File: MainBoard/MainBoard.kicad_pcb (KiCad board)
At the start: 6 copper layers, 45 x 45.6 mm, 93 parts, among them J1 KH-TYPE-C-16P, Q1 PMV19XNEAR, Q2 PMV19XNEAR, Q3 PMV19XNEAR, Q4 PMV19XNEAR, U2 SI3477DV-T1-GE3, U3 STM32L496VGY6PTR, U4 FUSB302BMPX, U5 BNO086, U6 TPS63802DLAR, U7 SI3477DV-T1-GE3, U8 BQ25756ERRVR, U9 TCAN332DCNR, Y1 9HT11-32.768KBZF-T

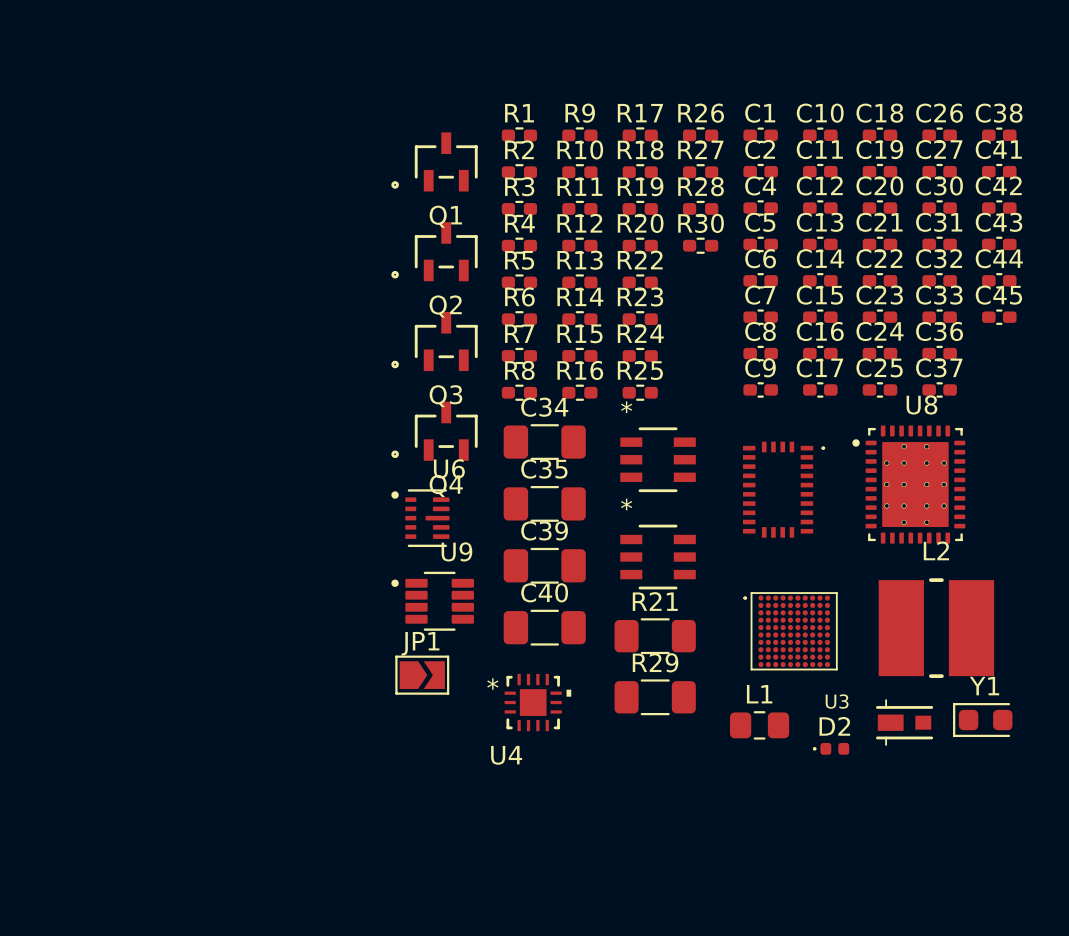
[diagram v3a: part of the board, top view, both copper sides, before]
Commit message: Adding cutoff circuits and others
Added 3.3V and Bat Voltage current sense and cutoff cirucits

Also changed footprints to non-hand solder for 0402

And changed I2C pullups to an array
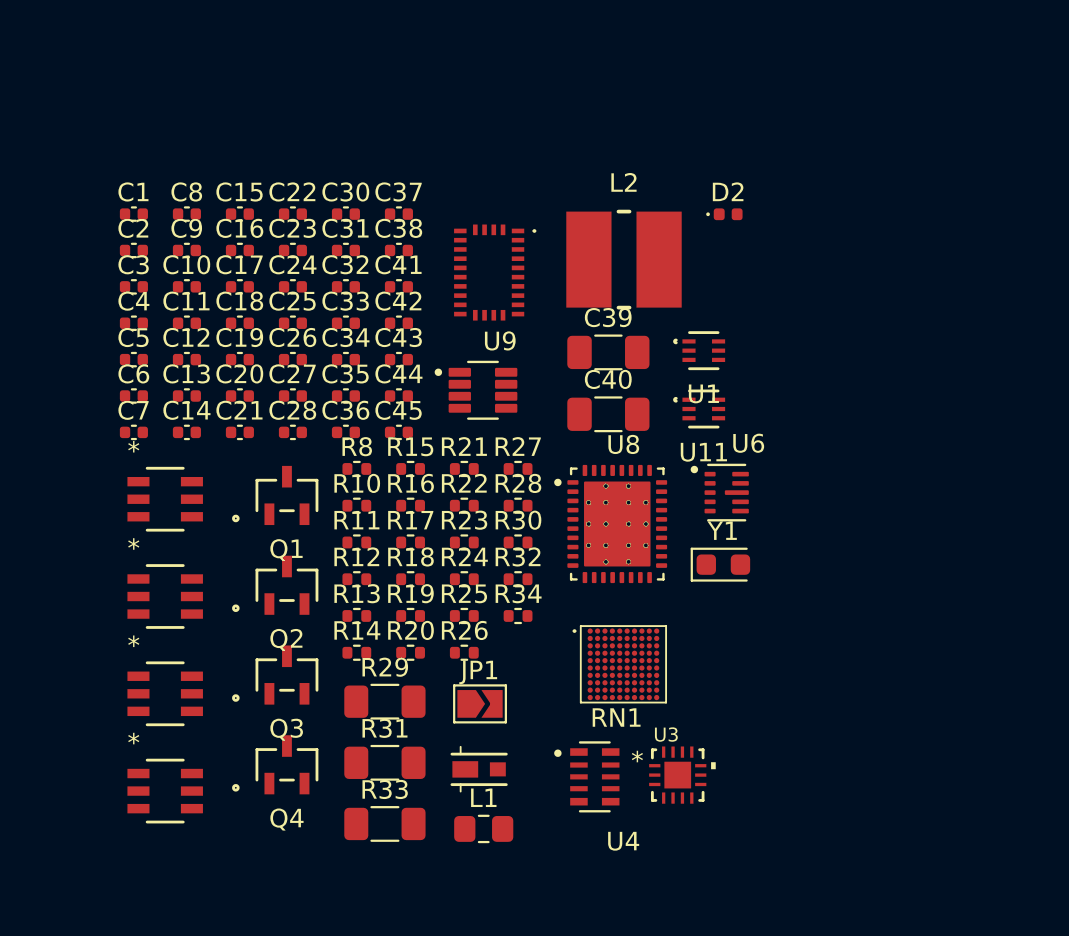
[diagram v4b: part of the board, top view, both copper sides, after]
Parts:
- removed R1, R2, R3, R4, R5, R6, R7, R9: 2.2k, Resistor_SMD:R_0402_1005Metric_Pad0.72x0.64mm_HandSolder
- added C28: 100nF, Capacitor_SMD:C_0402_1005Metric, F.Cu at (131.7, 61.5)
- added C3: 100nF, Capacitor_SMD:C_0402_1005Metric, F.Cu at (123.1, 53.6)
- added R31: 5m, Resistor_SMD:R_1206_3216Metric_Pad1.30x1.75mm_HandSolder, F.Cu at (136.7, 79.4)
- added R32: 100K, Resistor_SMD:R_0402_1005Metric, F.Cu at (143.9, 69.5)
- added R33: 5m, Resistor_SMD:R_1206_3216Metric_Pad1.30x1.75mm_HandSolder, F.Cu at (136.7, 82.7)
- added R34: 100K, Resistor_SMD:R_0402_1005Metric, F.Cu at (143.9, 71.5)
- added RN1: YC158TJR-072K2L, inspirefly:RESCAXE64P320X160X70-10N, F.Cu at (148.0, 80.2)
- added U1: INA185A4IDRLR, inspirefly:SOT_INA185_TEX, F.Cu at (153.9, 57.1)
- added U10: SI3477DV-T1-GE3, inspirefly:SOT_V-T1-GE3_VIS-M, F.Cu at (124.8, 75.7)
- added U11: INA185A4IDRLR, inspirefly:SOT_INA185_TEX, F.Cu at (153.9, 60.3)
- added U12: SI3477DV-T1-GE3, inspirefly:SOT_V-T1-GE3_VIS-M, F.Cu at (124.8, 80.9)
- C1, C10, C11, C12, C13, C14, C15, C16, C17, C18, C19, C2, C20, C21, C22, C23, C24, C25, C26, C27, C30, C31, C32, C33, C36, C37, C38, C4, C41, C42, C43, C44, C45, C5, C6, C7, C8, C9: footprint Capacitor_SMD:C_0402_1005Metric_Pad0.74x0.62mm_HandSolder -> Capacitor_SMD:C_0402_1005Metric
- C34, C35: footprint Capacitor_SMD:C_1206_3216Metric_Pad1.33x1.80mm_HandSolder -> Capacitor_SMD:C_0402_1005Metric
- R10, R11, R12, R13, R14, R15, R16, R17, R18, R19, R20, R22, R23, R24, R25, R26, R27, R28, R30, R8: footprint Resistor_SMD:R_0402_1005Metric_Pad0.72x0.64mm_HandSolder -> Resistor_SMD:R_0402_1005Metric
- R21: footprint Resistor_SMD:R_1206_3216Metric_Pad1.30x1.75mm_HandSolder -> Resistor_SMD:R_0402_1005Metric
- moved C26 37.1 mm to (131.7, 57.6)
- moved C27 37.1 mm to (131.7, 59.6)
- moved C18 36.1 mm to (128.8, 55.6)
- moved C19 36.1 mm to (128.8, 57.6)
- moved C20 36.1 mm to (128.8, 59.6)
- moved C21 36.1 mm to (128.8, 61.5)
- moved C11 35.3 mm to (126.0, 55.6)
- moved C10 35.3 mm to (126.0, 53.6)
- moved C12 35.3 mm to (126.0, 57.6)
- moved C13 35.3 mm to (126.0, 59.6)
- moved C14 35.3 mm to (126.0, 61.5)
- moved C4 34.5 mm to (123.1, 55.6)
- moved C5 34.5 mm to (123.1, 57.6)
- moved C6 34.5 mm to (123.1, 59.6)
- moved C7 34.5 mm to (123.1, 61.5)
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
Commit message: Footprint edits and board setup
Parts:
- removed C24, C25: 22pF, Capacitor_SMD:C_0402_1005Metric
- removed Y1: 9HT11-32.768KBZF-T, Crystal:Crystal_SMD_2012-2Pin_2.0x1.2mm_HandSoldering
- added TP1: BatBeforeCutoff, TestPoint:TestPoint_Pad_D1.0mm, F.Cu at (155.0, 71.9)
- added TP2: Bat+, TestPoint:TestPoint_Pad_D1.0mm, F.Cu at (155.0, 74.9)
- added TP3: 3.3V, TestPoint:TestPoint_Pad_D1.0mm, F.Cu at (158.1, 71.9)
- added TP4: GND, TestPoint:TestPoint_Pad_D1.0mm, F.Cu at (158.1, 74.9)
- added TP5: GND, TestPoint:TestPoint_Pad_D1.0mm, F.Cu at (161.1, 71.9)
- added TP6: GND, TestPoint:TestPoint_Pad_D1.0mm, F.Cu at (161.1, 74.9)
- JP1: footprint Jumper:SolderJumper-2_P1.3mm_Open_TrianglePad1.0x1.5mm -> inspirefly:SmallJumper
- R19: value 25k -> 50k
- moved U3 59.0 mm to (92.4, 59.6)
- moved R33 36.0 mm to (155.4, 51.9)
- moved R29 36.0 mm to (155.4, 45.3)
- moved R31 36.0 mm to (155.4, 48.6)
- moved D1 33.7 mm to (160.5, 51.7)
- moved D2 28.1 mm to (159.9, 77.4)
- moved Q1 26.5 mm to (150.1, 46.1)
- moved U10 26.5 mm to (143.5, 56.8)
- moved Q2 26.5 mm to (150.1, 51.0)
- moved Q3 26.5 mm to (150.1, 55.8)
- moved Q4 26.5 mm to (150.1, 60.7)
- moved U2 26.5 mm to (143.5, 46.3)
- moved U7 26.5 mm to (143.5, 51.6)
- moved U12 26.5 mm to (143.5, 62.1)
- moved U5 23.0 mm to (150.0, 74.5)
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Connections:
- C41 pad 2: GND -> Net-(U8-BTST1)
- C42 pad 1: GND -> BAT_SIDE_INDUC
- C42 pad 2: BAT_SIDE_INDUC -> Net-(U8-BTST2)
- U3 pad E1: unconnected-(U3A-PC8-PadE1) -> IMU_MCO
- U5 pad 10: unconnected-(U5-CLKSEL0-Pad10) -> +3.3V
- U5 pad 17: unconnected-(U5-SA0/H_MOSI-Pad17) -> H_MDSI_MCUMOSI
- U5 pad 18: unconnected-(U5-H_CSN-Pad18) -> IMU_CSN_GPIO
- U5 pad 19: unconnected-(U5-H_SCL/SCK/RX-Pad19) -> IMU_MCU_SLK
- U5 pad 20: unconnected-(U5-H_SDA/H_MISO/TX-Pad20) -> IMU_MCU_MISO
- U5 pad 26: Net-(U5-XOUT32/CLKSEL1) -> +3.3V
- U5 pad 27: Net-(U5-XIN32) -> IMU_MCO
- U8 pad 20: BAT_SIDE_INDUC -> Net-(U8-BTST2)
- U8 pad 26: EXTERNAL_SIDE_INDUC -> Net-(U8-BTST1)

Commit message: Added a good amount of STM connections
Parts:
- added C24: 100nF, Capacitor_SMD:C_0402_1005Metric, F.Cu at (136.7, 81.4)
- added C25: 100nF, Capacitor_SMD:C_0402_1005Metric, F.Cu at (136.7, 83.3)
- added R1: 1k, Resistor_SMD:R_0402_1005Metric, F.Cu at (133.8, 81.4)
- added R2: 1k, Resistor_SMD:R_0402_1005Metric, F.Cu at (133.8, 83.4)
- moved U11 4.76 mm to (165.2, 47.6)
- moved U8 1.84 mm to (158.1, 57.8)
- moved U1 1.43 mm to (160.9, 43.9)
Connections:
- U3 pad A3: unconnected-(U3A-PD1-PadA3) -> CAN_TXD
- U3 pad A5: unconnected-(U3A-PG10-PadA5) -> PARENT_SPI3_MISO
- U3 pad A7: unconnected-(U3A-PB6-PadA7) -> I2C4_SCL
- U3 pad A8: unconnected-(U3A-PB9-PadA8) -> I2C1_SDA
- U3 pad B3: unconnected-(U3A-PD0-PadB3) -> CAN_RXD
- U3 pad B6: unconnected-(U3A-PG12-PadB6) -> PARENT_SPI3_NSS
- U3 pad B7: unconnected-(U3A-PB7-PadB7) -> I2C4_SDA
- U3 pad B8: unconnected-(U3A-PB8-PadB8) -> I2C1_SCL
- U3 pad C1: unconnected-(U3A-PA12-PadC1) -> USB_D+
- U3 pad D1: unconnected-(U3A-PA11-PadD1) -> USB_D-
- U3 pad D6: unconnected-(U3A-PG9-PadD6) -> PARENT_SPI3_SCK
- U3 pad E5: unconnected-(U3A-PG11-PadE5) -> PARENT_SPI3_MOSI
- U3 pad F6: unconnected-(U3A-PC3-PadF6) -> ANT_SPI2_MOSI
- U3 pad F7: unconnected-(U3A-PC1-PadF7) -> I2C3_SDA
- U3 pad G10: unconnected-(U3A-PC0-PadG10) -> I2C3_SCL
- U3 pad G6: unconnected-(U3A-PA7-PadG6) -> H_MDSI_SPI1_MOSI
- U3 pad G7: unconnected-(U3A-PA1-PadG7) -> Net-(U3A-PA1)
- U3 pad G8: IMU_PS0/WAKE_GPIO -> unconnected-(U3A-PA0-PadG8)
- U3 pad G9: unconnected-(U3A-PC2-PadG9) -> ANT_SPI2_MISO
- U3 pad H1: unconnected-(U3A-PB14-PadH1) -> I2C2_SDA
- U3 pad H2: unconnected-(U3A-PB13-PadH2) -> I2C2_SCL
- U3 pad H7: unconnected-(U3A-PA4-PadH7) -> IMU_SP1_NSS
- U3 pad H8: unconnected-(U3A-PA2-PadH8) -> Net-(U3A-PA2)
- U3 pad J1: unconnected-(U3A-PB12-PadJ1) -> ANT_SPI2_NSS
- U3 pad J7: unconnected-(U3A-PA5-PadJ7) -> IMU_MCU_SPI1_SCK
- U3 pad K3: unconnected-(U3A-PB10-PadK3) -> ANT_SPI2_SCK
- U3 pad K9: unconnected-(U3A-PA6-PadK9) -> IMU_MCU_SPI1_MISO
- U5 pad 17: H_MDSI_MCUMOSI -> H_MDSI_SPI1_MOSI
- U5 pad 18: IMU_CSN_GPIO -> IMU_SP1_NSS
- U5 pad 19: IMU_MCU_SLK -> IMU_MCU_SPI1_SCK
- U5 pad 20: IMU_MCU_MISO -> IMU_MCU_SPI1_MISO
- U5 pad 26: +3.3V -> GND
- U5 pad 27: IMU_MCO -> unconnected-(U5-XIN32-Pad27)

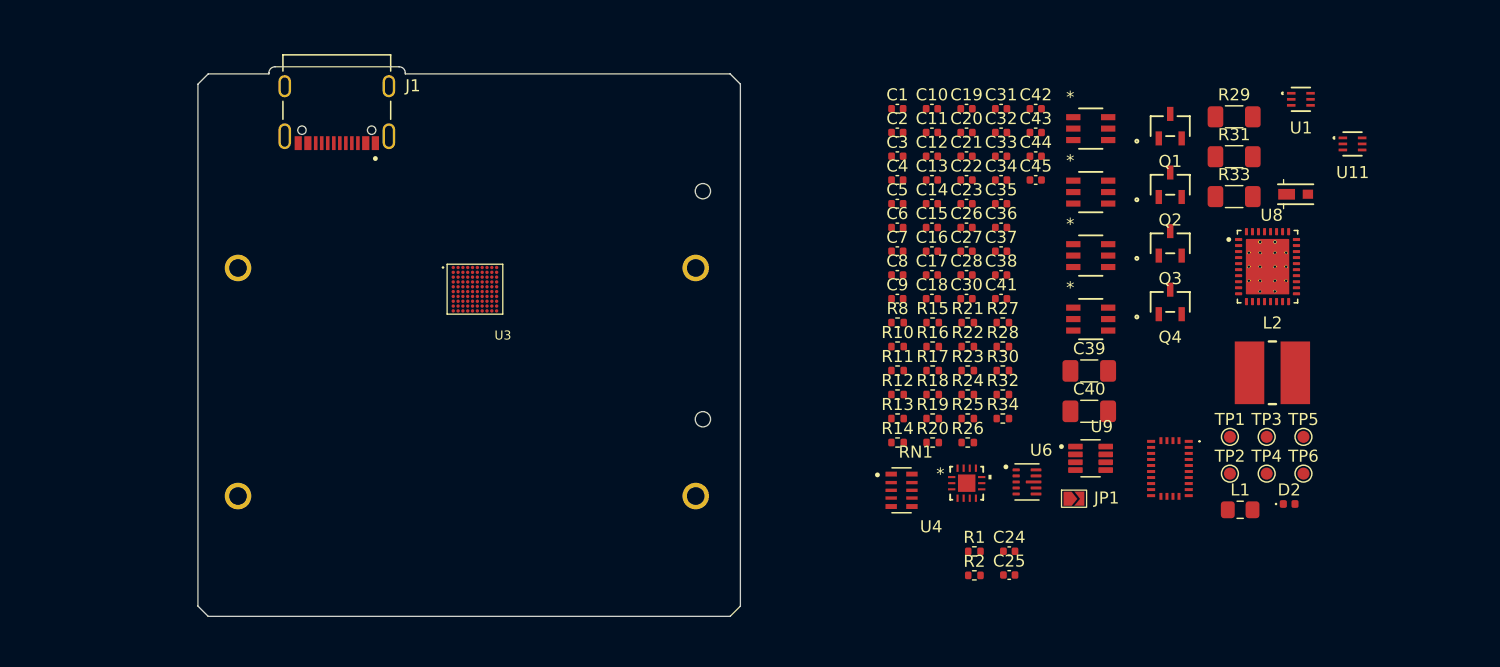
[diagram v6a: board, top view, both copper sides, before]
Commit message: Pushing more schematic changes
Added ST link connections
Added Harwin M55
Changed some items for Battery managment
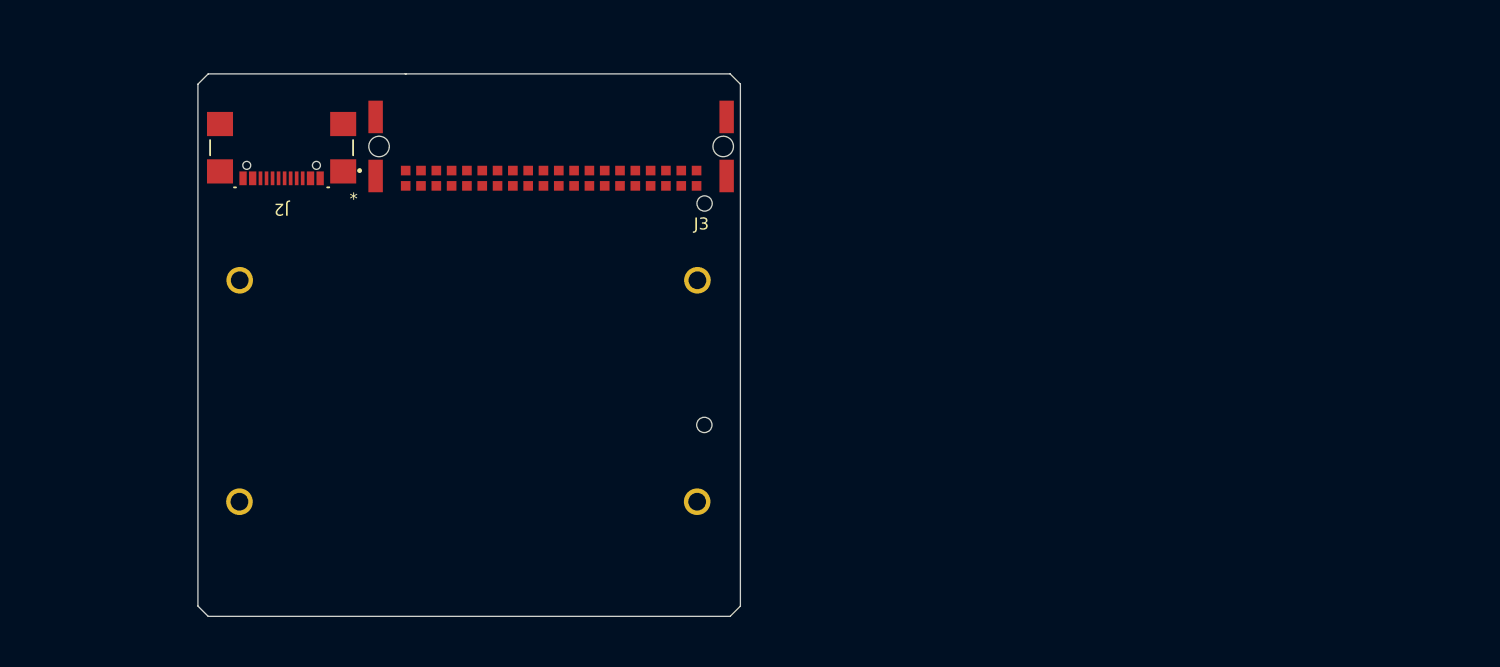
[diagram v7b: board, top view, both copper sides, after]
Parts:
- removed C1, C16, C19, C38, C9: 1uF, Capacitor_SMD:C_0402_1005Metric
- removed C10, C11, C36, C37: 4.7uF, Capacitor_SMD:C_0402_1005Metric
- removed C12, C13, C14, C15, C17, C2, C20, C21, C22, C23, C24, C25, C28, C3, C30, C32, C33, C4, C41, C42, C43, C45, C5: 100nF, Capacitor_SMD:C_0402_1005Metric
- removed C18, C26, C27: 10uF, Capacitor_SMD:C_0402_1005Metric
- removed C31, C44: 470nF, Capacitor_SMD:C_0402_1005Metric
- removed C34, C35: 47uF, Capacitor_SMD:C_0402_1005Metric
- removed C39, C40: 47uF, Capacitor_SMD:C_1206_3216Metric_Pad1.33x1.80mm_HandSolder
- removed C6, C7: 470pF, Capacitor_SMD:C_0402_1005Metric
- removed C8: 10nF, Capacitor_SMD:C_0402_1005Metric
- removed D1: MSS2P2-M3/89A, inspirefly:DIODE_MSP3V3
- removed D2: LED, LED_SMD:LED_0402_1005Metric
- removed J1: KH-TYPE-C-16P, inspirefly:KINGHELM_KH-TYPE-C-16P
- removed JP1: Footswitch_Disable, inspirefly:SmallJumper
- removed L1: 470nH, Inductor_SMD:L_0805_2012Metric_Pad1.15x1.40mm_HandSolder
- removed L2: 4.7uH, inspirefly:WE-LQSA_5040
- removed Q1, Q2, Q3, Q4: PMV19XNEAR, inspirefly:TO-236AB_SOT23_NEX
- removed R1, R2: 1k, Resistor_SMD:R_0402_1005Metric
- removed R10, R24, R26: 10k, Resistor_SMD:R_0402_1005Metric
- removed R11: 280k, Resistor_SMD:R_0402_1005Metric
- removed R12, R19: 50k, Resistor_SMD:R_0402_1005Metric
- removed R13, R32, R34: 100K, Resistor_SMD:R_0402_1005Metric
- removed R14: 143k, Resistor_SMD:R_0402_1005Metric
- removed R15, R22: 250k, Resistor_SMD:R_0402_1005Metric
- removed R16: 6.2k, Resistor_SMD:R_0402_1005Metric
- removed R17: 36k, Resistor_SMD:R_0402_1005Metric
- removed R18, R23, R27, R28, R30: 10, Resistor_SMD:R_0402_1005Metric
- removed R20: 40k, Resistor_SMD:R_0402_1005Metric
- removed R21: 5m, Resistor_SMD:R_0402_1005Metric
- removed R25: 120, Resistor_SMD:R_0402_1005Metric
- removed R29, R31, R33: 5m, Resistor_SMD:R_1206_3216Metric_Pad1.30x1.75mm_HandSolder
- removed R8: 2.2k, Resistor_SMD:R_0402_1005Metric
- removed RN1: YC158TJR-072K2L, inspirefly:RESCAXE64P320X160X70-10N
- removed TP1: BatBeforeCutoff, TestPoint:TestPoint_Pad_D1.0mm
- removed TP2: Bat+, TestPoint:TestPoint_Pad_D1.0mm
- removed TP3: 3.3V, TestPoint:TestPoint_Pad_D1.0mm
- removed TP4, TP5, TP6: GND, TestPoint:TestPoint_Pad_D1.0mm
- removed U1, U11: INA185A4IDRLR, inspirefly:SOT_INA185_TEX
- removed U10, U12, U2, U7: SI3477DV-T1-GE3, inspirefly:SOT_V-T1-GE3_VIS-M
- removed U3: STM32L496VGY6PTR, inspirefly:STM32L496VGY6TR
- removed U4: FUSB302BMPX, inspirefly:MLP14_2P5X2P5_ONS
- removed U5: BNO086, inspirefly:BNO086
- removed U6: TPS63802DLAR, inspirefly:VREG_TPS63802DLAR
- removed U8: BQ25756ERRVR, inspirefly:IC_BQ25756ERRVR
- removed U9: TCAN332DCNR, inspirefly:SOT65P280X145-8N
- added J2: USB4110-GF-A, inspirefly:USB4110-GF-A_GCT, F.Cu at (76.3, 47.1)
- added J3: M55-7104042R, inspirefly:HARWIN_M55-7104042R, F.Cu at (98.7, 47.8)
- moved BT2 19.4 mm to (91.8, 77.2)
- moved BT1 17.9 mm to (91.8, 58.9)
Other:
- board size 45 x 45.6 mm -> 45 x 45 mm
